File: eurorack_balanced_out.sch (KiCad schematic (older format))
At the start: 20 parts

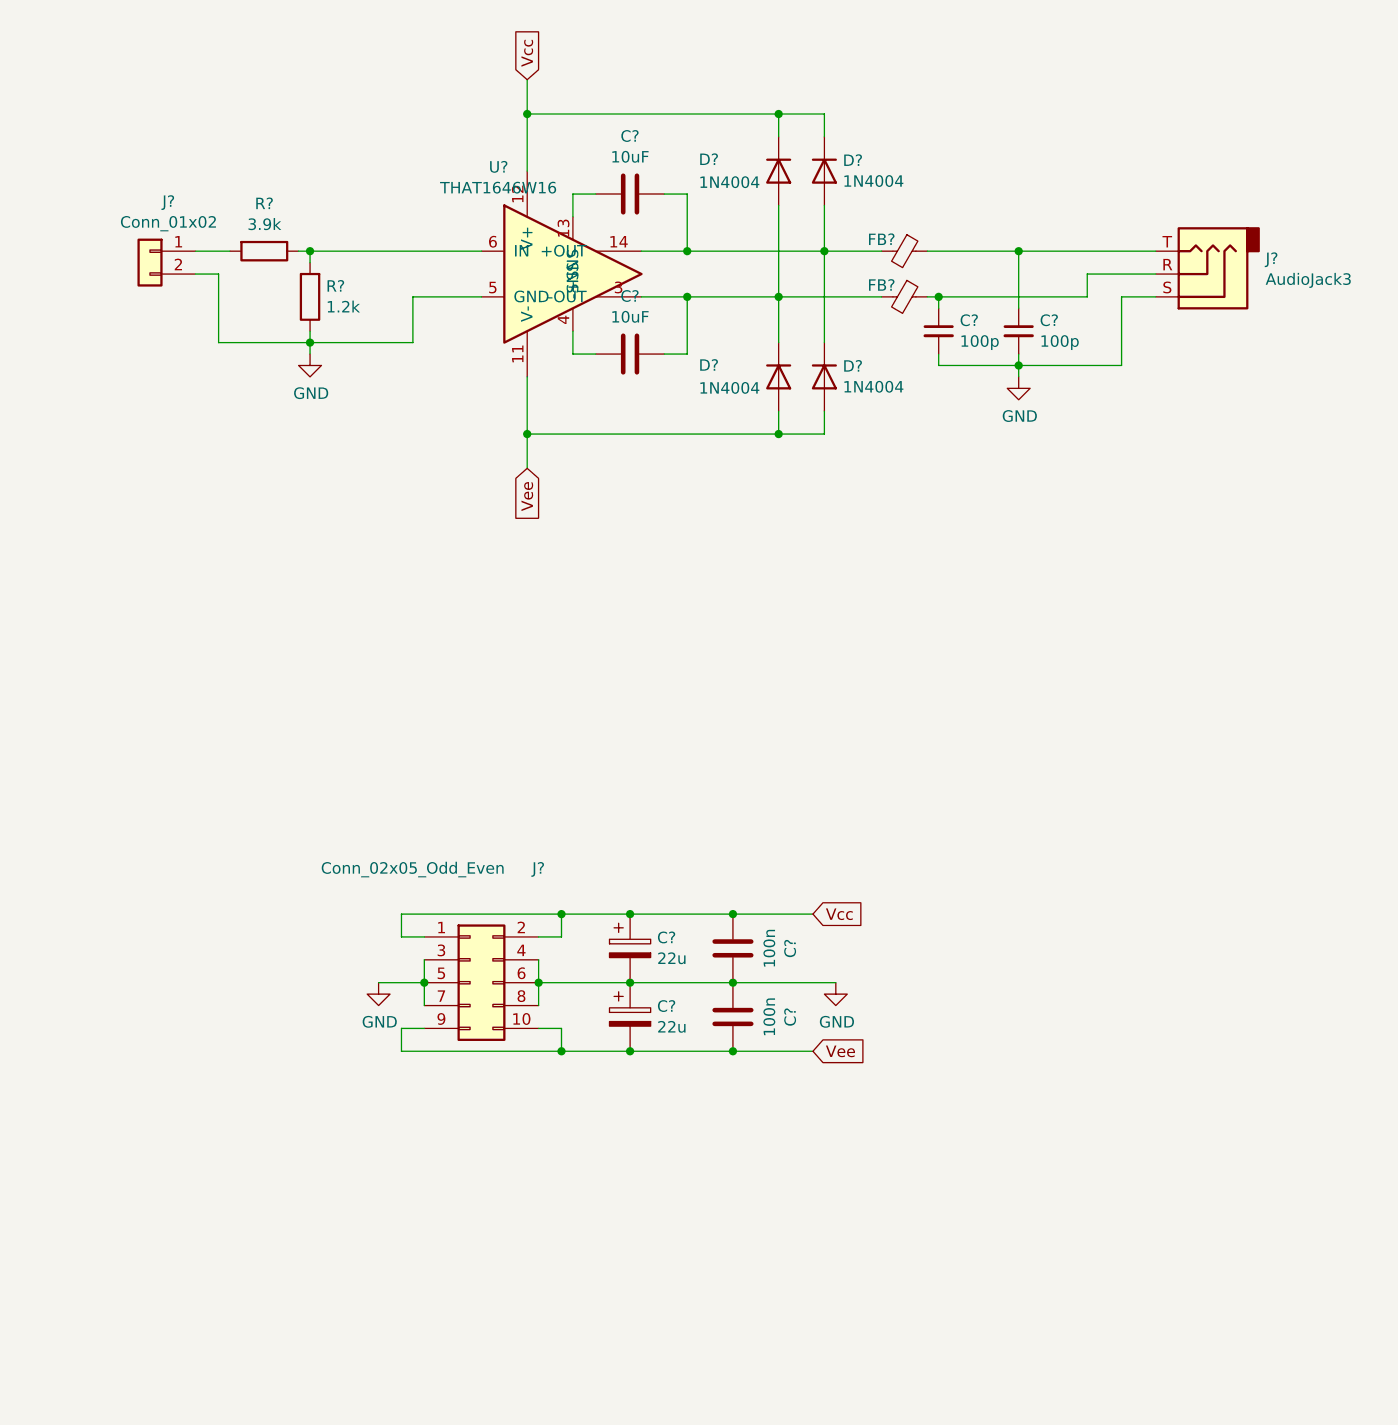
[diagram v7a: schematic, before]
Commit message: re-add second channel
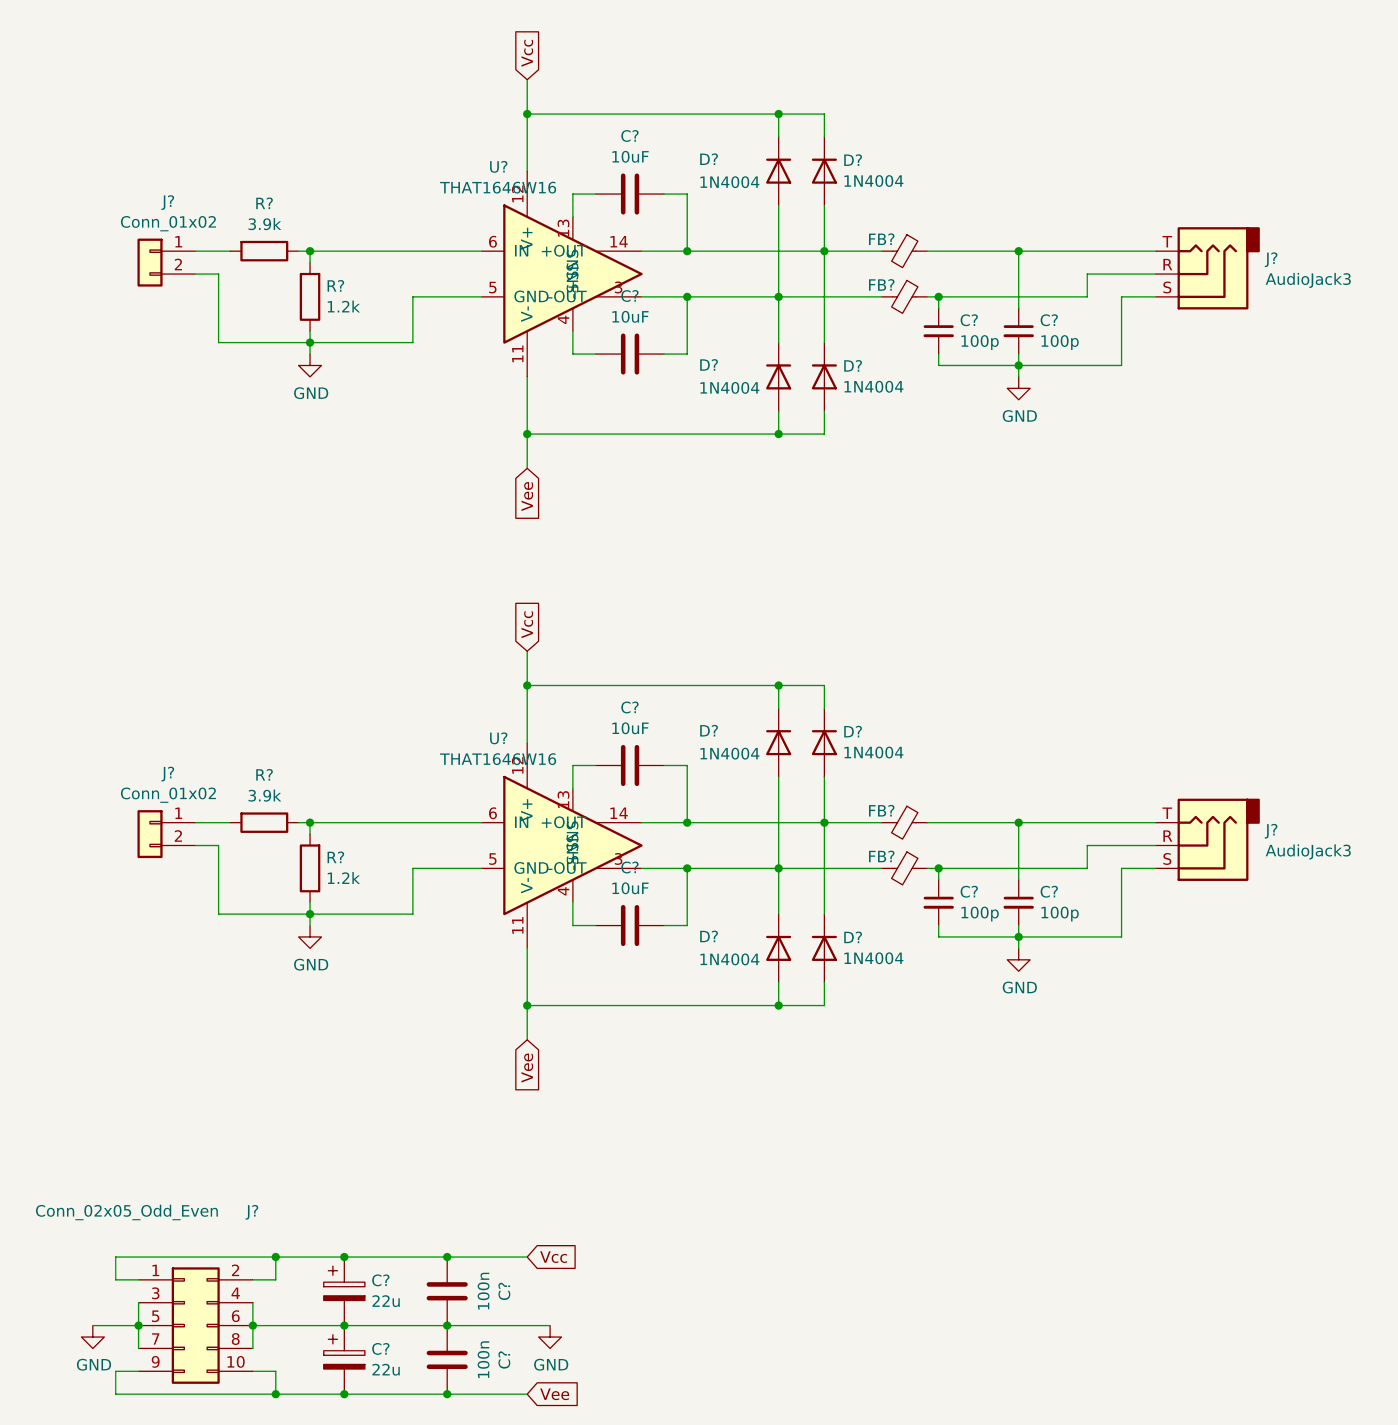
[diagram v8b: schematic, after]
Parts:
- added C? (x2): 10uF, Capacitor_SMD:CP_Elec_5x5.4, symbol Device:C
- added C? (x2): 100p, Capacitor_SMD:C_0805_2012Metric_Pad1.15x1.40mm_HandSolder, symbol Device:C_Small
- added D? (x4): 1N4004, Diode_THT:D_DO-41_SOD81_P10.16mm_Horizontal, symbol Diode:1N4004
- added FB? (x2): 600R @ 100Mhz, Resistor_SMD:R_0805_2012Metric_Pad1.15x1.40mm_HandSolder, symbol Device:Ferrite_Bead_Small
- added J?: Conn_01x02, symbol Connector_Generic:Conn_01x02
- added J?: AudioJack3, Connector_Audio:Jack_6.35mm_Neutrik_NJ3FD-V_Vertical, symbol Connector:AudioJack3
- added R?: 3.9k, Resistor_SMD:R_0805_2012Metric_Pad1.15x1.40mm_HandSolder, symbol Device:R
- added R?: 1.2k, Resistor_SMD:R_0805_2012Metric_Pad1.15x1.40mm_HandSolder, symbol Device:R
- added U?: THAT1646W16, Package_SO:SOIC-16W_7.5x10.3mm_P1.27mm, symbol patchut:THAT1646W16
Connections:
- net GND: now also C?.2, C?.2, J?.2 (Pin_2), J?.S, R?.1, U?.5 (GND)
- net Vcc: now also D?.1 (K), D?.1 (K), U?.12 (V+)
- net Vee: now also D?.2 (A), D?.2 (A), U?.11 (V-)
- new net: U?.1 (nc1), U?.10 (nc6), U?.15 (nc7), U?.16 (nc8), U?.2 (nc2), U?.7 (nc3), U?.8 (nc4), U?.9 (nc5)
- new net: C?.2, U?.13 (+SNS)
- new net: C?.1, D?.1 (K), D?.2 (A), FB?.2, U?.14 (+OUT)
- new net: C?.1, D?.1 (K), D?.2 (A), FB?.2, U?.3 (-OUT)
- new net: C?.2, U?.4 (-SNS)
- new net: R?.1, R?.2, U?.6 (IN)
- new net: J?.1 (Pin_1), R?.2
- new net: C?.1, FB?.1, J?.R
- new net: C?.1, FB?.1, J?.T
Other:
- moved on the sheet: C?, J?
